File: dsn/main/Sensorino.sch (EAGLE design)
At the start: 45 parts, among them IC1 LDO3V3

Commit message: Added PTH render
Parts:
- Q1: value (none) -> 16Mhz
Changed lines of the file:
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@@
 <part name="C1" library="SparkFun-Capacitors" deviceset="0.1UF-50V-20%(PTH)" device="KIT-EZ" value="0.1uF"/>
 <part name="GND2" library="SparkFun-Aesthetics" deviceset="GND" device=""/>
-<part name="Q1" library="special" deviceset="XTAL/S" device=""/>
+<part name="Q1" library="special" deviceset="XTAL/S" device="" value="16Mhz"/>
 <part name="C2" library="SparkFun-Capacitors" deviceset="0.1UF-50V-20%(PTH)" device="KIT-EZ" value="18pF"/>
 <part name="C3" library="SparkFun-Capacitors" deviceset="0.1UF-50V-20%(PTH)" device="KIT-EZ" value="18pF"/>

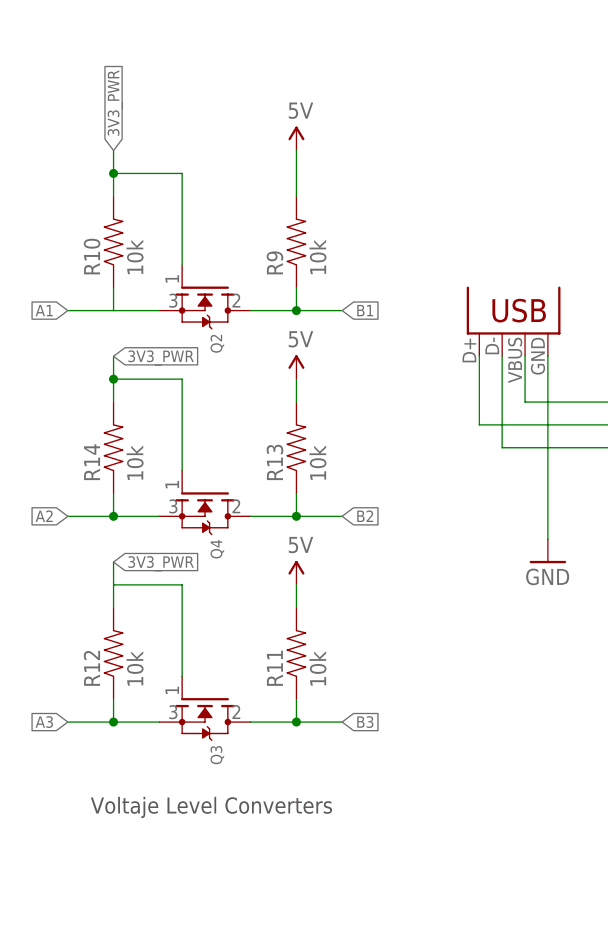
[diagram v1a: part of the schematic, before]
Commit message: Mosfet changed to a more-acceptable model
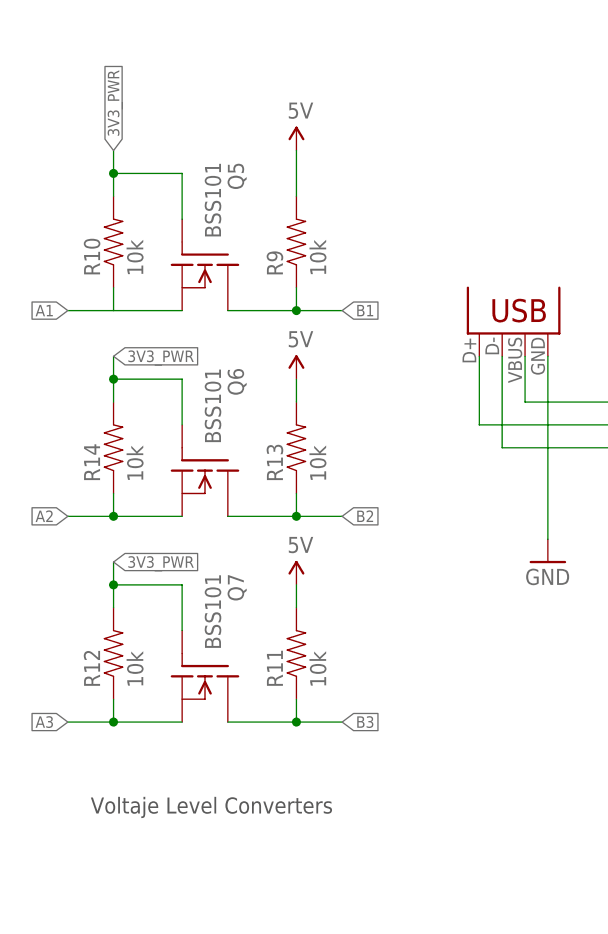
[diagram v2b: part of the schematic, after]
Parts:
- removed Q2, Q3, Q4: (no value), adafruit:MOSFET-NGDS_TO220V
- added Q5, Q6, Q7: BSS101, transistor-fet:BSS101
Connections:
- net 3V3_PWR: now also Q5.G, Q6.G, Q7.G; no longer Q2.G, Q3.G, Q4.G
- net A1: now also Q5.S; no longer Q2.S
- net A2: now also Q6.S; no longer Q4.S
- net A3: now also Q7.S; no longer Q3.S
- net B1: now also Q5.D; no longer Q2.D
- net B2: now also Q6.D; no longer Q4.D
- net B3: now also Q7.D; no longer Q3.D
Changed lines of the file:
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@@
 <part name="C4" library="SparkFun-Capacitors" deviceset="0.1UF-50V-20%(PTH)" device="KIT-EZ" value="22pF"/>
 <part name="C5" library="SparkFun-Capacitors" deviceset="0.1UF-50V-20%(PTH)" device="KIT-EZ" value="22pF"/>
-<part name="Q2" library="adafruit" deviceset="MOSFET-N" device="GDS_TO220V"/>
-<part name="Q3" library="adafruit" deviceset="MOSFET-N" device="GDS_TO220V"/>
-<part name="Q4" library="adafruit" deviceset="MOSFET-N" device="GDS_TO220V"/>
 <part name="R9" library="SparkFun-Resistors" deviceset="RESISTOR" device="AXIAL-0.3" value="10k"/>
 <part name="R10" library="SparkFun-Resistors" deviceset="RESISTOR" device="AXIAL-0.3" value="10k"/>
@@
 <part name="R18" library="SparkFun-Resistors" deviceset="RESISTOR" device="AXIAL-0.3" value="470"/>
 <part name="R19" library="SparkFun-Resistors" deviceset="RESISTOR" device="AXIAL-0.3" value="470"/>
+<part name="Q5" library="transistor-fet" deviceset="BSS101" device=""/>
+<part name="Q6" library="transistor-fet" deviceset="BSS101" device=""/>
+<part name="Q7" library="transistor-fet" deviceset="BSS101" device=""/>
 </parts>
 <sheets>
@@
 <instance part="C4" gate="G$1" x="-165.1" y="-43.18"/>
 <instance part="C5" gate="G$1" x="-139.7" y="-43.18"/>
-<instance part="Q2" gate="G$1" x="-223.52" y="43.18" rot="R270"/>
-<instance part="Q3" gate="G$1" x="-223.52" y="-2.54" rot="R270"/>
-<instance part="Q4" gate="G$1" x="-223.52" y="20.32" rot="R270"/>
 <instance part="R9" gate="G$1" x="-213.36" y="48.26" rot="R90"/>
 <instance part="R10" gate="G$1" x="-233.68" y="48.26" rot="R90"/>
@@
 <instance part="R18" gate="G$1" x="-220.98" y="-63.5" rot="R180"/>
 <instance part="R19" gate="G$1" x="-220.98" y="-73.66" rot="R180"/>
+<instance part="Q5" gate="G$1" x="-223.52" y="45.72" rot="R270"/>
+<instance part="Q6" gate="G$1" x="-223.52" y="22.86" rot="R270"/>
+<instance part="Q7" gate="G$1" x="-223.52" y="0" rot="R270"/>
 </instances>
 <busses>
@@
 <pinref part="R10" gate="G$1" pin="2"/>
 <wire x1="-233.68" y1="53.34" x2="-233.68" y2="55.88" width="0.1524" layer="91"/>
-<pinref part="Q2" gate="G$1" pin="G"/>
-<wire x1="-226.06" y1="45.72" x2="-226.06" y2="55.88" width="0.1524" layer="91"/>
 <wire x1="-226.06" y1="55.88" x2="-233.68" y2="55.88" width="0.1524" layer="91"/>
 <wire x1="-233.68" y1="55.88" x2="-233.68" y2="58.42" width="0.1524" layer="91"/>
 <junction x="-233.68" y="55.88"/>
 <label x="-233.68" y="58.42" size="1.27" layer="95" rot="R90" xref="yes"/>
+<pinref part="Q5" gate="G$1" pin="G"/>
+<wire x1="-226.06" y1="55.88" x2="-226.06" y2="50.8" width="0.1524" layer="91"/>
 </segment>
 <segment>
 <pinref part="R14" gate="G$1" pin="2"/>
 <wire x1="-233.68" y1="35.56" x2="-233.68" y2="33.02" width="0.1524" layer="91"/>
-<pinref part="Q4" gate="G$1" pin="G"/>
 <wire x1="-233.68" y1="33.02" x2="-233.68" y2="30.48" width="0.1524" layer="91"/>
 <wire x1="-233.68" y1="33.02" x2="-226.06" y2="33.02" width="0.1524" layer="91"/>
-<wire x1="-226.06" y1="33.02" x2="-226.06" y2="22.86" width="0.1524" layer="91"/>
+<wire x1="-226.06" y1="33.02" x2="-226.06" y2="27.94" width="0.1524" layer="91"/>
 <junction x="-233.68" y="33.02"/>
 <label x="-233.68" y="35.56" size="1.27" layer="95" xref="yes"/>
+<pinref part="Q6" gate="G$1" pin="G"/>
 </segment>
 <segment>
 <pinref part="R12" gate="G$1" pin="2"/>
 <wire x1="-233.68" y1="12.7" x2="-233.68" y2="10.16" width="0.1524" layer="91"/>
-<pinref part="Q3" gate="G$1" pin="G"/>
 <wire x1="-233.68" y1="10.16" x2="-233.68" y2="7.62" width="0.1524" layer="91"/>
 <wire x1="-233.68" y1="10.16" x2="-226.06" y2="10.16" width="0.1524" layer="91"/>
-<wire x1="-226.06" y1="10.16" x2="-226.06" y2="0" width="0.1524" layer="91"/>
 <label x="-233.68" y="12.7" size="1.27" layer="95" xref="yes"/>
+<pinref part="Q7" gate="G$1" pin="G"/>
+<wire x1="-226.06" y1="10.16" x2="-226.06" y2="5.08" width="0.1524" layer="91"/>
+<junction x="-233.68" y="10.16"/>
 </segment>
 <segment>
@@
 <segment>
 <pinref part="R9" gate="G$1" pin="1"/>
-<pinref part="Q2" gate="G$1" pin="D"/>
 <wire x1="-213.36" y1="43.18" x2="-213.36" y2="40.64" width="0.1524" layer="91"/>
-<wire x1="-213.36" y1="40.64" x2="-218.44" y2="40.64" width="0.1524" layer="91"/>
+<wire x1="-213.36" y1="40.64" x2="-220.98" y2="40.64" width="0.1524" layer="91"/>
 <wire x1="-213.36" y1="40.64" x2="-208.28" y2="40.64" width="0.1524" layer="91"/>
 <label x="-208.28" y="40.64" size="1.27" layer="95" xref="yes"/>
 <junction x="-213.36" y="40.64"/>
+<pinref part="Q5" gate="G$1" pin="D"/>
 </segment>
 <segment>
@@
 <segment>
 <pinref part="R10" gate="G$1" pin="1"/>
-<pinref part="Q2" gate="G$1" pin="S"/>
 <wire x1="-233.68" y1="43.18" x2="-233.68" y2="40.64" width="0.1524" layer="91"/>
-<wire x1="-233.68" y1="40.64" x2="-228.6" y2="40.64" width="0.1524" layer="91"/>
+<wire x1="-233.68" y1="40.64" x2="-226.06" y2="40.64" width="0.1524" layer="91"/>
 <wire x1="-233.68" y1="40.64" x2="-238.76" y2="40.64" width="0.1524" layer="91"/>
 <label x="-238.76" y="40.64" size="1.27" layer="95" rot="R180" xref="yes"/>
+<pinref part="Q5" gate="G$1" pin="S"/>
 </segment>
 <segment>
@@
 <net name="A2" class="0">
 <segment>
-<pinref part="Q4" gate="G$1" pin="S"/>
 <pinref part="R14" gate="G$1" pin="1"/>
-<wire x1="-228.6" y1="17.78" x2="-233.68" y2="17.78" width="0.1524" layer="91"/>
+<wire x1="-226.06" y1="17.78" x2="-233.68" y2="17.78" width="0.1524" layer="91"/>
 <wire x1="-233.68" y1="17.78" x2="-233.68" y2="20.32" width="0.1524" layer="91"/>
 <junction x="-233.68" y="17.78"/>
 <wire x1="-233.68" y1="17.78" x2="-238.76" y2="17.78" width="0.1524" layer="91"/>
 <label x="-238.76" y="17.78" size="1.27" layer="95" rot="R180" xref="yes"/>
+<pinref part="Q6" gate="G$1" pin="S"/>
 </segment>
 <segment>
@@
 <net name="B2" class="0">
 <segment>
-<pinref part="Q4" gate="G$1" pin="D"/>
 <pinref part="R13" gate="G$1" pin="1"/>
-<wire x1="-218.44" y1="17.78" x2="-213.36" y2="17.78" width="0.1524" layer="91"/>
+<wire x1="-220.98" y1="17.78" x2="-213.36" y2="17.78" width="0.1524" layer="91"/>
 <wire x1="-213.36" y1="17.78" x2="-213.36" y2="20.32" width="0.1524" layer="91"/>
 <junction x="-213.36" y="17.78"/>
 <wire x1="-213.36" y1="17.78" x2="-208.28" y2="17.78" width="0.1524" layer="91"/>
 <label x="-208.28" y="17.78" size="1.27" layer="95" xref="yes"/>
+<pinref part="Q6" gate="G$1" pin="D"/>
 </segment>
 <segment>
@@
 <segment>
 <pinref part="R12" gate="G$1" pin="1"/>
-<pinref part="Q3" gate="G$1" pin="S"/>
 <wire x1="-233.68" y1="-2.54" x2="-233.68" y2="-5.08" width="0.1524" layer="91"/>
-<wire x1="-233.68" y1="-5.08" x2="-228.6" y2="-5.08" width="0.1524" layer="91"/>
+<wire x1="-233.68" y1="-5.08" x2="-226.06" y2="-5.08" width="0.1524" layer="91"/>
 <junction x="-233.68" y="-5.08"/>
 <wire x1="-233.68" y1="-5.08" x2="-238.76" y2="-5.08" width="0.1524" layer="91"/>
 <label x="-238.76" y="-5.08" size="1.27" layer="95" rot="R180" xref="yes"/>
+<pinref part="Q7" gate="G$1" pin="S"/>
 </segment>
 <segment>
@@
 <net name="B3" class="0">
 <segment>
-<pinref part="Q3" gate="G$1" pin="D"/>
 <pinref part="R11" gate="G$1" pin="1"/>
-<wire x1="-218.44" y1="-5.08" x2="-213.36" y2="-5.08" width="0.1524" layer="91"/>
+<wire x1="-220.98" y1="-5.08" x2="-213.36" y2="-5.08" width="0.1524" layer="91"/>
 <wire x1="-213.36" y1="-5.08" x2="-213.36" y2="-2.54" width="0.1524" layer="91"/>
 <junction x="-213.36" y="-5.08"/>
 <wire x1="-213.36" y1="-5.08" x2="-208.28" y2="-5.08" width="0.1524" layer="91"/>
 <label x="-208.28" y="-5.08" size="1.27" layer="95" xref="yes"/>
-</segment>
-<segment>
+<pinref part="Q7" gate="G$1" pin="D"/>
+</segment>
+<segment>
